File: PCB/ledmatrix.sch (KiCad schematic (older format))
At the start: 84 parts

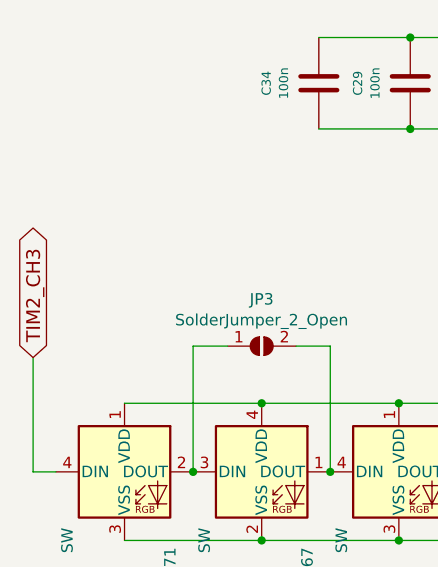
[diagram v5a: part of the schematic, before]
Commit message: Correct RGB DATA
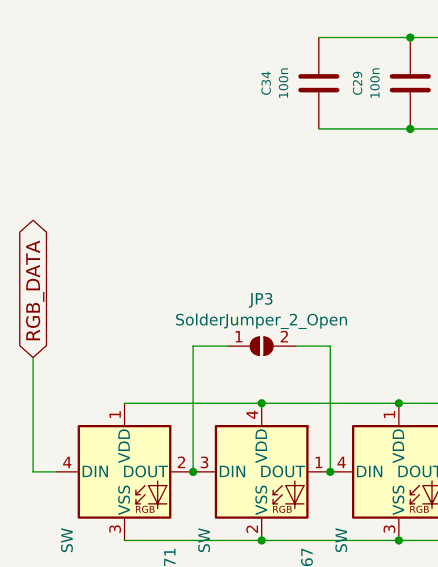
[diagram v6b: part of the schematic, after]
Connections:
- net TIM2_CH3 renamed RGB_DATA
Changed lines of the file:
@@
 $EndComp
 Text GLabel 700  3300 1    60   BiDi ~ 0
-TIM2_CH3
+RGB_DATA
 NoConn ~ 8950 3950
 $Comp

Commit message: YAEMK 1.2 RC
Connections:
- net VDD renamed RGB_VDD
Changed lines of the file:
@@
-$EndComp
-$Comp
-L YAEMK:VDD #PWR06
-U 1 1 5FB0F6DB
-P 6350 700
-F 0 "#PWR06" H 6350 800 30  0001 C CNN
-F 1 "VDD" H 6364 838 30  0000 C CNN
-F 2 "" H 6350 700 60  0000 C CNN
-F 3 "" H 6350 700 60  0000 C CNN
-	1    6350 700
-	1    0    0    -1
 $EndComp
 $Comp
@@
 F 3 "" H 9550 2100 60  0000 C CNN
 	1    9550 2100
-	1    0    0    -1
-$EndComp
-$Comp
-L YAEMK:VDD #PWR0101
-U 1 1 60053F25
-P 6350 1750
-F 0 "#PWR0101" H 6350 1850 30  0001 C CNN
-F 1 "VDD" H 6364 1888 30  0000 C CNN
-F 2 "" H 6350 1750 60  0000 C CNN
-F 3 "" H 6350 1750 60  0000 C CNN
-	1    6350 1750
 	1    0    0    -1
 $EndComp
@@
 	5300 3500 5900 3500
 Connection ~ 5900 3500
-Wire Wire Line
-	5900 3500 6200 3500
 Connection ~ 6500 3500
 Wire Wire Line
@@
 Connection ~ 5250 5100
 Wire Wire Line
-	5250 5100 5850 5100
+	5250 5100 5550 5100
 Connection ~ 5850 5100
-Wire Wire Line
-	5850 5100 6200 5100
 Connection ~ 6450 5100
 Wire Wire Line
@@
 Connection ~ 2850 5550
 Wire Wire Line
-	2850 5550 2500 5550
-Wire Wire Line
 	1050 6150 1650 6150
 Connection ~ 1650 6150
@@
 Wire Wire Line
 	700  3800 700  3300
-$Comp
-L YAEMK:VDD #PWR0104
-U 1 1 601B1A63
-P 6200 3500
-F 0 "#PWR0104" H 6200 3600 30  0001 C CNN
-F 1 "VDD" H 6214 3638 30  0000 C CNN
-F 2 "" H 6200 3500 60  0000 C CNN
-F 3 "" H 6200 3500 60  0000 C CNN
-	1    6200 3500
-	1    0    0    -1
-$EndComp
-Connection ~ 6200 3500
-Wire Wire Line
-	6200 3500 6500 3500
-$Comp
-L YAEMK:VDD #PWR0105
-U 1 1 601B2BDA
-P 6200 5100
-F 0 "#PWR0105" H 6200 5200 30  0001 C CNN
-F 1 "VDD" H 6214 5238 30  0000 C CNN
-F 2 "" H 6200 5100 60  0000 C CNN
-F 3 "" H 6200 5100 60  0000 C CNN
-	1    6200 5100
-	-1   0    0    1
-$EndComp
-Connection ~ 6200 5100
-Wire Wire Line
-	6200 5100 6450 5100
-$Comp
-L YAEMK:VDD #PWR0106
-U 1 1 601B8FE4
-P 2500 5550
-F 0 "#PWR0106" H 2500 5650 30  0001 C CNN
-F 1 "VDD" H 2514 5688 30  0000 C CNN
-F 2 "" H 2500 5550 60  0000 C CNN
-F 3 "" H 2500 5550 60  0000 C CNN
-	1    2500 5550
-	1    0    0    -1
-$EndComp
-Connection ~ 2500 5550
-Wire Wire Line
-	2500 5550 2250 5550
 $Comp
 L YAEMK:VSS #PWR0107
@@
 	1950 5300 2100 5300
 Connection ~ 1950 4800
+Wire Wire Line
+	5900 3500 6200 3500
+Wire Wire Line
+	5850 5100 6450 5100
+Text GLabel 6200 3250 1    50   Input ~ 0
+RGB_VDD
+Wire Wire Line
+	6200 3250 6200 3500
+Connection ~ 6200 3500
+Wire Wire Line
+	6200 3500 6500 3500
+Text GLabel 5550 5250 3    50   Input ~ 0
+RGB_VDD
+Wire Wire Line
+	5550 5100 5550 5250
+Connection ~ 5550 5100
+Wire Wire Line
+	5550 5100 5850 5100
+Wire Wire Line
+	2250 5550 2850 5550
+Text GLabel 2850 5350 2    50   Input ~ 0
+RGB_VDD
+Wire Wire Line
+	2850 5350 2850 5550
+Text GLabel 6350 700  2    50   Input ~ 0
+RGB_VDD
+Text GLabel 6350 1750 2    50   Input ~ 0
+RGB_VDD
 $EndSCHEMATC

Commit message: Clean up save point
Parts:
- removed JP3, JP4, JP5, JP6, JP7, JP8: SolderJumper_2_Open, prettylib:SOLDER_JUMPER_2, symbol Jumper:SolderJumper_2_Open
- D35, D37, D38, D39, D40, D42, D44, D45, D46, D47, D48, D49, D50, D51, D52, D53, D54, D55, D56, D57, D58, D60, D61, D63, D64, D66, D67, D71, D72, D73, D74, D75, D76: footprint prettylib:SK6812_mini_e_flippable -> prettylib:SK6812_mini_e_flipable
